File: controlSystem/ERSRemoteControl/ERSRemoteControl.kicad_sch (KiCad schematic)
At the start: 54 parts, among them J1 USB_C_Receptacle_USB2.0_14P, J2 0022-232041, J5 0022-232021, J6 0022-232021, J7 0022-232031, SW2 SW_Push, SW3 SW_Push, SW4 SW_Push, SW5 SW_Push, SW6 SW_Push, SW7 SW_Push, U1 TPS63070, U2 ESP32-S3-WROOM-1

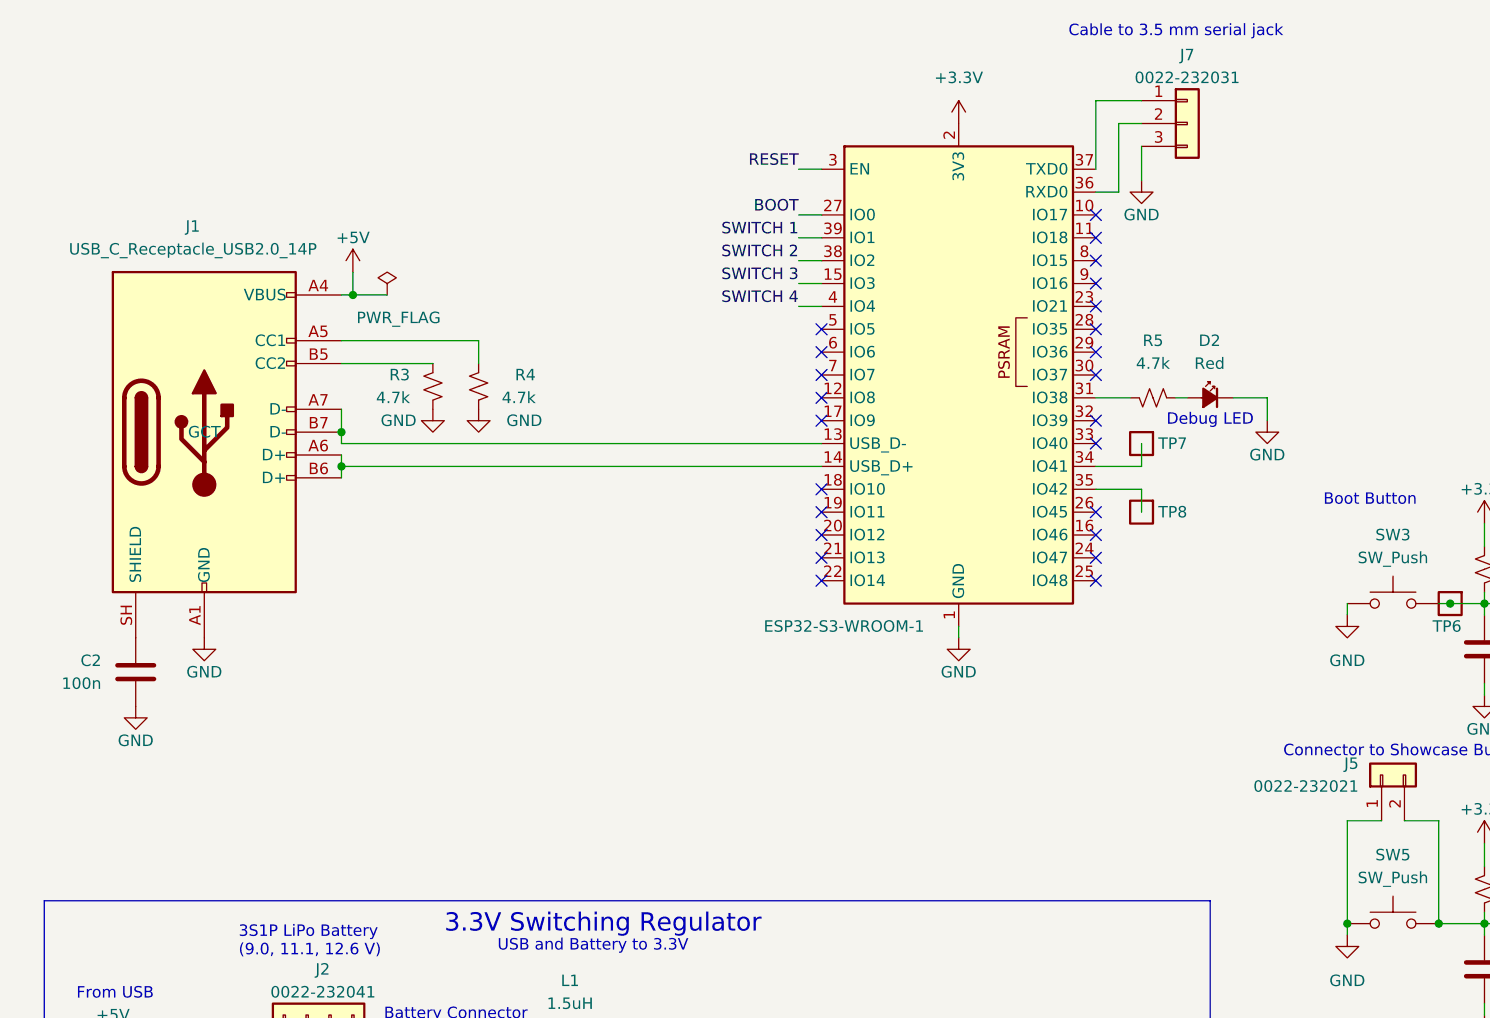
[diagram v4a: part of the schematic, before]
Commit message: Fixed traces, removed the mode switch and added debouncing logic
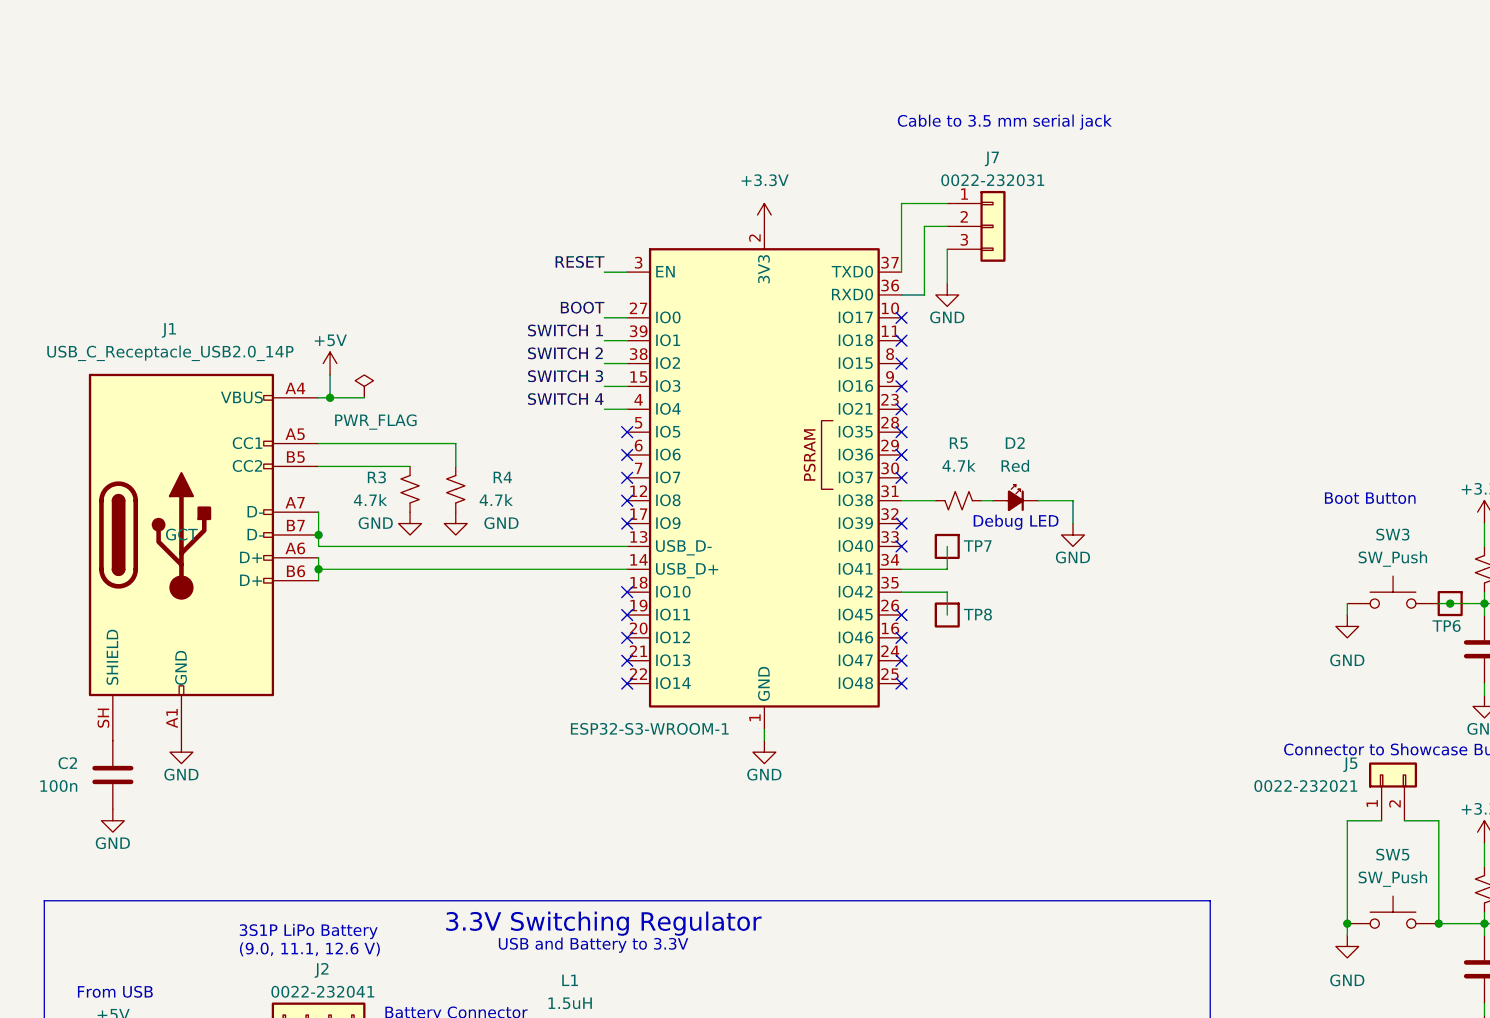
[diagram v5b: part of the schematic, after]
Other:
- moved on the sheet: C2, D2, J1, J7, R3, R4, R5, TP7, TP8

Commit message: Design review, set board constraints to osh park two layer, fix library paths, etc
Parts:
- TP1, TP2, TP3, TP4, TP5, TP6, TP7, TP8: symbol psas-testpoint:Test-Point -> Connector:TestPoint_Square
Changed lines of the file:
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@@
 	)
 	(symbol
-		(lib_id "psas-testpoint:Test-Point")
+		(lib_id "Connector:TestPoint_Square")
 		(at 118.11 78.74 0)
 		(mirror y)
@@
 	)
 	(symbol
-		(lib_id "psas-testpoint:Test-Point")
+		(lib_id "Connector:TestPoint_Square")
 		(at 208.28 77.47 0)
 		(mirror y)
@@
 	)
 	(symbol
-		(lib_id "psas-testpoint:Test-Point")
+		(lib_id "Connector:TestPoint_Square")
 		(at 91.44 158.75 0)
 		(unit 1)
@@
 	)
 	(symbol
-		(lib_id "psas-testpoint:Test-Point")
+		(lib_id "Connector:TestPoint_Square")
 		(at 91.44 148.59 0)
 		(unit 1)
@@
 	)
 	(symbol
-		(lib_id "psas-testpoint:Test-Point")
+		(lib_id "Connector:TestPoint_Square")
 		(at 173.99 77.47 0)
 		(mirror y)
@@
 	)
 	(symbol
-		(lib_id "psas-testpoint:Test-Point")
+		(lib_id "Connector:TestPoint_Square")
 		(at 118.11 71.12 0)
 		(mirror y)
@@
 	)
 	(symbol
-		(lib_id "psas-testpoint:Test-Point")
+		(lib_id "Connector:TestPoint_Square")
 		(at 76.2 171.45 0)
 		(unit 1)
@@
 		(dnp no)
 		(property "Reference" "TP3"
-			(at 74.93 173.99 0)
+			(at 77.978 172.72 0)
 			(show_name no)
 			(do_not_autoplace no)
@@
 	)
 	(symbol
-		(lib_id "psas-testpoint:Test-Point")
+		(lib_id "Connector:TestPoint_Square")
 		(at 106.68 135.89 0)
 		(unit 1)

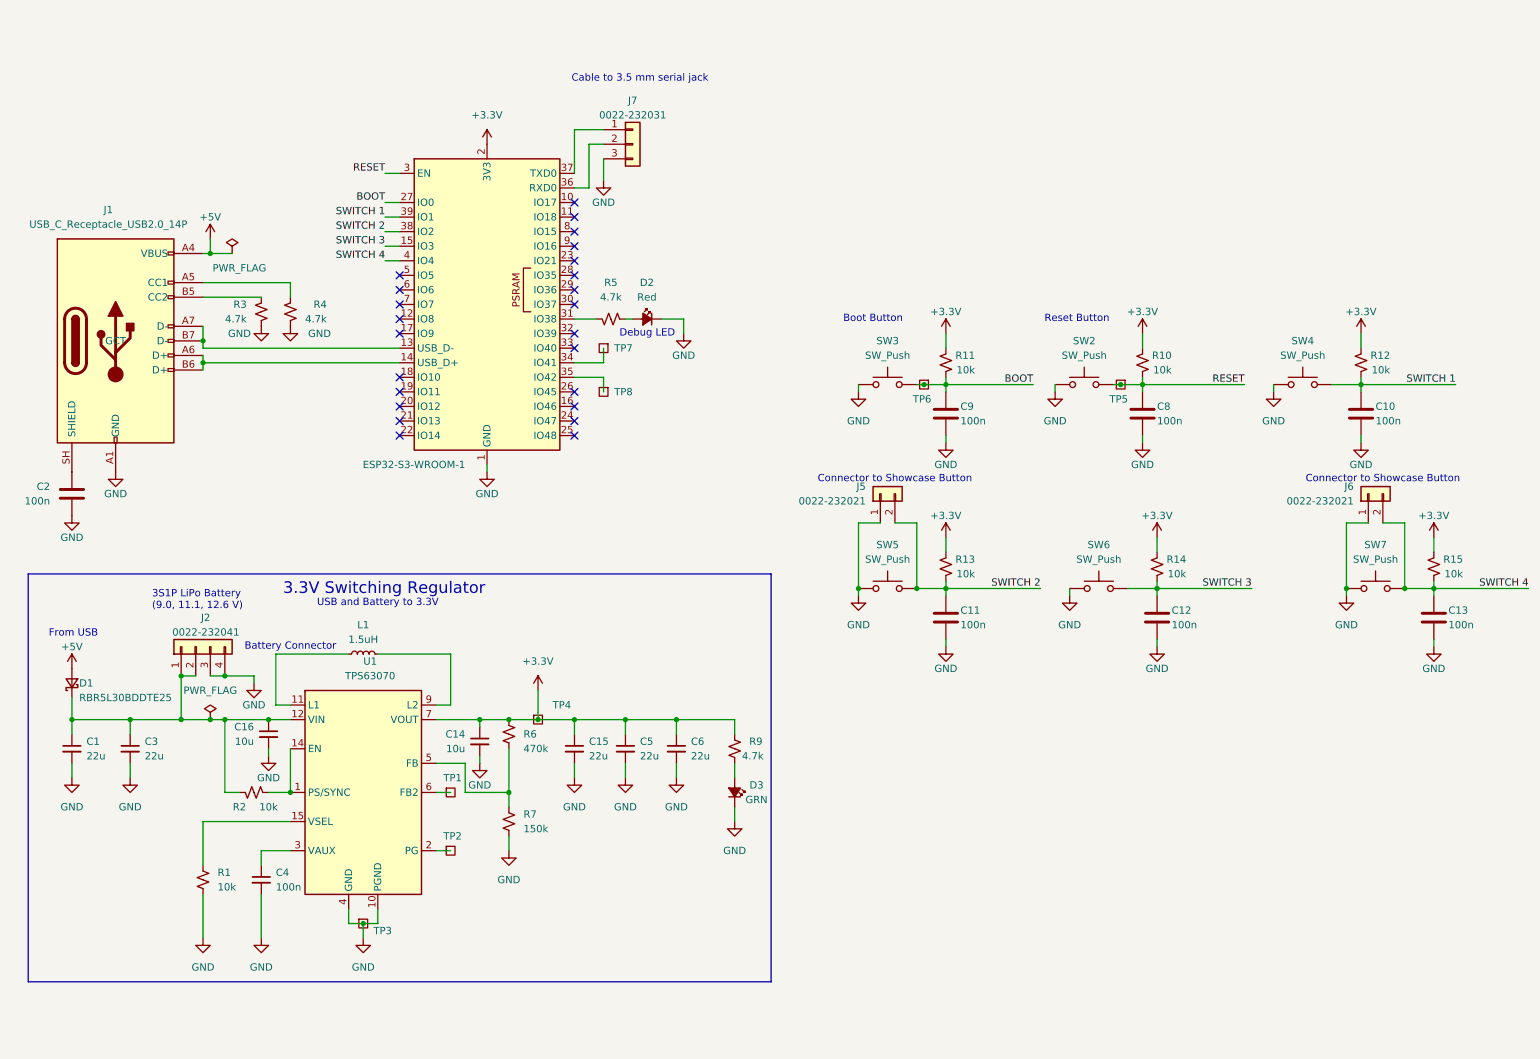
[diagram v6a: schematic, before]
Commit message: Fixed library issues and completed design review changes
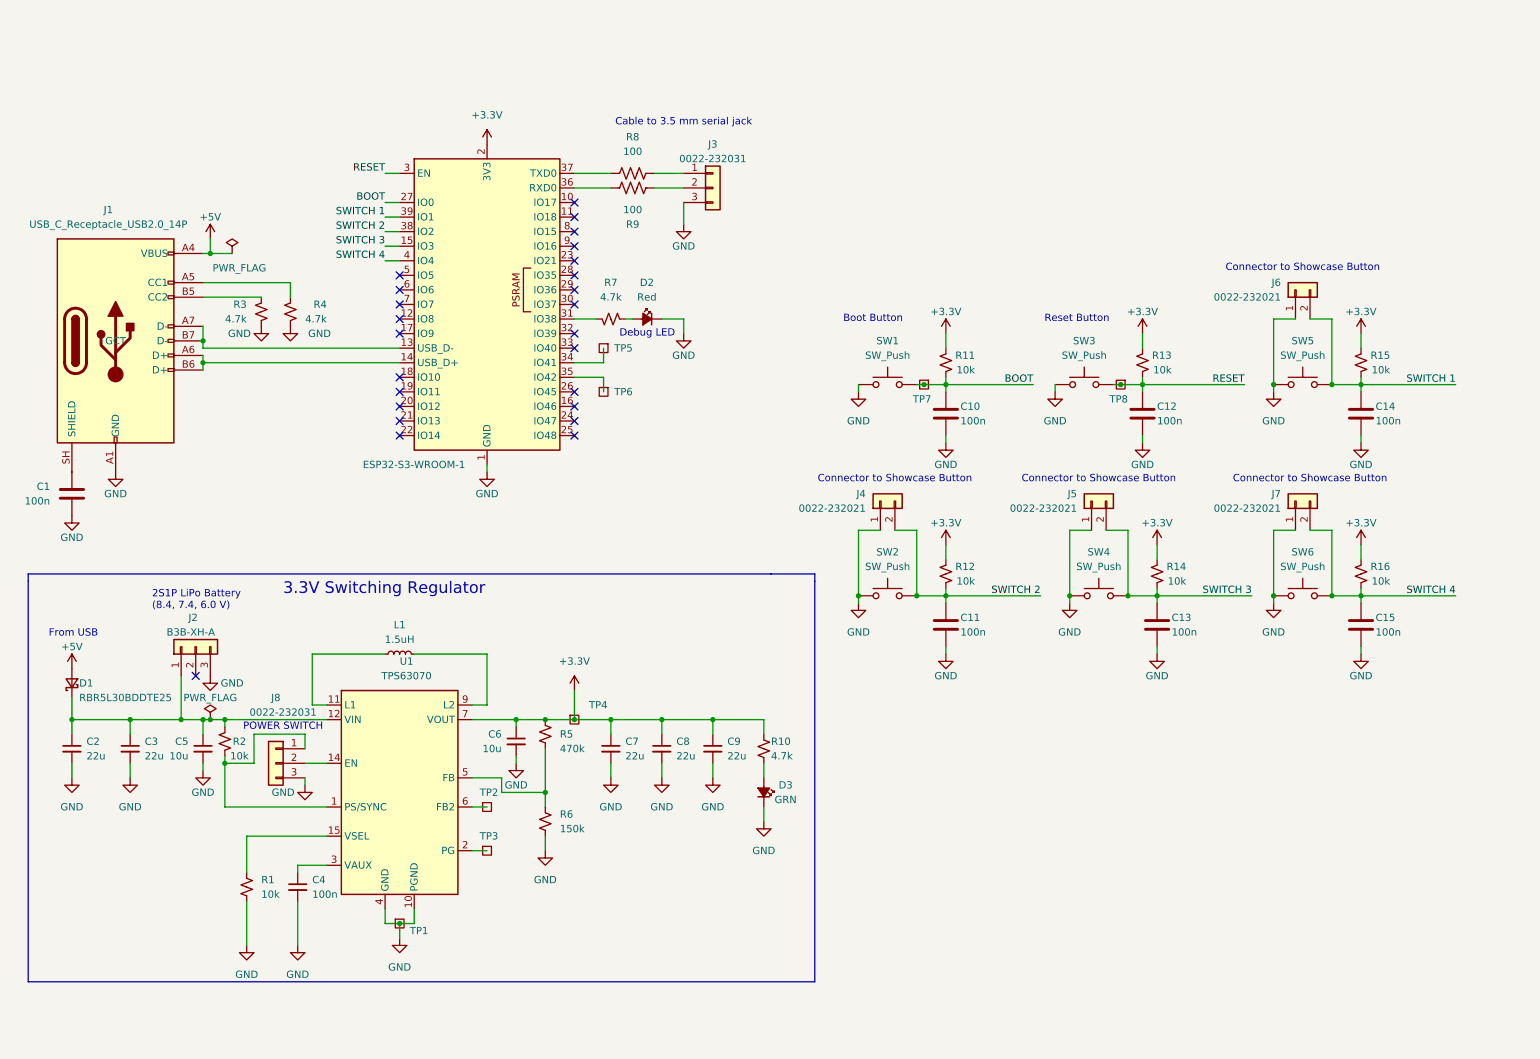
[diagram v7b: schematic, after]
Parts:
- removed J2: 0022-232041, Connector_Molex:Molex_KK-254_AE-6410-04A_1x04_P2.54mm_Vertical, symbol Connector_Generic:Conn_01x04
- added J2: B3B-XH-A, Connector_JST:JST_XH_B3B-XH-A_1x03_P2.50mm_Vertical, symbol Connector_Generic:Conn_01x03
- added J5, J6: 0022-232021, Connector_Molex:Molex_KK-254_AE-6410-02A_1x02_P2.54mm_Vertical, symbol Connector_Generic:Conn_01x02
- added J8: 0022-232031, Connector_Molex:Molex_KK-254_AE-6410-03A_1x03_P2.54mm_Vertical, symbol Connector_Generic:Conn_01x03
- added R8, R9: 100, Resistor_SMD:R_0603_1608Metric, symbol Device:R_US
- renumbered C2 to C1, C9 to C10, C8 to C12, C12 to C13, C10 to C14, C13 to C15, C1 to C2, C16 to C5, C14 to C6, C15 to C7, C5 to C8, C6 to C9, J7 to J3, J5 to J4, J6 to J7, R9 to R10, R13 to R12, R10 to R13, R12 to R15, R15 to R16, R6 to R5, R7 to R6, R5 to R7, SW3 to SW1, SW5 to SW2, SW2 to SW3, SW6 to SW4, SW4 to SW5, SW7 to SW6, TP3 to TP1, TP1 to TP2, TP2 to TP3, TP7 to TP5, TP8 to TP6, TP6 to TP7, TP5 to TP8
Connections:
- net GND: now also J2.3 (Pin_3), J5.1 (Pin_1), J6.1 (Pin_1), J8.3 (Pin_3)
- net SWITCH 1: now also J6.2 (Pin_2)
- net SWITCH 3: now also J5.2 (Pin_2)
- net at C2.1, C3.1, C5.1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: now also R2.2, J2.1 (Pin_1); no longer R2.1
- net at J3.2 (Pin_2): now also R9.1; no longer U2.36 (RXD0)
- net at U2.37 (TXD0): now also R8.1; no longer J3.1 (Pin_1)
- new net: J8.1 (Pin_1), R2.1, U1.1 (PS/SYNC)
- new net: J8.2 (Pin_2), U1.14 (EN)
- new net: J3.1 (Pin_1), R8.2
- new net: R9.2, U2.36 (RXD0)
- no-connect marks 24 -> 25
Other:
- note added: "2S1P LiPo Battery (8.4, 7.4, 6.0 V)"
- note added: "POWER SWITCH"
- note removed: "3S1P LiPo Battery (9.0, 11.1, 12.6 V)"
- note removed: "Battery Connector"
- note removed: "USB and Battery to 3.3V"
- moved on the sheet: C11, C13, C15, C4, C5, C6, C7, C8, C9, D3, J3, J4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

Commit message: Made the traces prettier but still not pretty
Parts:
- J2: DPN (none) -> 455-2248-ND; DST (none) -> DigiKey; MFR (none) -> JST; MPN (none) -> B3B-XH-A
- R8, R9: DPN (none) -> 311-100HRCT-ND; DST (none) -> DigiKey; MFR (none) -> Yageo; MPN (none) -> RC0603FR-07100RL
- TP5, TP6: now left out of the parts list
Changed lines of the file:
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@@
 		(body_style 1)
 		(exclude_from_sim no)
-		(in_bom yes)
+		(in_bom no)
 		(on_board yes)
 		(in_pos_files yes)
@@
 		(body_style 1)
 		(exclude_from_sim no)
-		(in_bom yes)
+		(in_bom no)
 		(on_board yes)
 		(in_pos_files yes)
@@
 			)
 		)
+		(property "DPN" "455-2248-ND"
+			(at 46.99 123.19 90)
+			(hide yes)
+			(show_name no)
+			(do_not_autoplace no)
+			(effects
+				(font
+					(size 1.27 1.27)
+				)
+			)
+		)
+		(property "DST" "DigiKey"
+			(at 46.99 123.19 90)
+			(hide yes)
+			(show_name no)
+			(do_not_autoplace no)
+			(effects
+				(font
+					(size 1.27 1.27)
+				)
+			)
+		)
+		(property "MFR" "JST"
+			(at 46.99 123.19 90)
+			(hide yes)
+			(show_name no)
+			(do_not_autoplace no)
+			(effects
+				(font
+					(size 1.27 1.27)
+				)
+			)
+		)
+		(property "MPN" "B3B-XH-A"
+			(at 46.99 123.19 90)
+			(hide yes)
+			(show_name no)
+			(do_not_autoplace no)
+			(effects
+				(font
+					(size 1.27 1.27)
+				)
+			)
+		)
 		(pin "3"
 		)
@@
 			)
 		)
+		(property "DPN" "311-100HRCT-ND"
+			(at 123.19 40.64 90)
+			(hide yes)
+			(show_name no)
+			(do_not_autoplace no)
+			(effects
+				(font
+					(size 1.27 1.27)
+				)
+			)
+		)
+		(property "DST" "DigiKey"
+			(at 123.19 40.64 90)
+			(hide yes)
+			(show_name no)
+			(do_not_autoplace no)
+			(effects
+				(font
+					(size 1.27 1.27)
+				)
+			)
+		)
+		(property "MFR" "Yageo"
+			(at 123.19 40.64 90)
+			(hide yes)
+			(show_name no)
+			(do_not_autoplace no)
+			(effects
+				(font
+					(size 1.27 1.27)
+				)
+			)
+		)
+		(property "MPN" "RC0603FR-07100RL"
+			(at 123.19 40.64 90)
+			(hide yes)
+			(show_name no)
+			(do_not_autoplace no)
+			(effects
+				(font
+					(size 1.27 1.27)
+				)
+			)
+		)
 		(pin "1"
 		)
@@
 			(hide yes)
 			(show_name no)
+			(do_not_autoplace no)
+			(effects
+				(font
+					(size 1.27 1.27)
+				)
+			)
+		)
+		(property "DPN" "311-100HRCT-ND"
+			(at 123.19 43.18 90)
+			(hide yes)
+			(show_name no)
+			(do_not_autoplace no)
+			(effects
+				(font
+					(size 1.27 1.27)
+				)
+			)
+		)
+		(property "DST" "DigiKey"
+			(at 123.19 43.18 90)
+			(hide yes)
+			(show_name no)
+			(do_not_autoplace no)
+			(effects
+				(font
+					(size 1.27 1.27)
+				)
+			)
+		)
+		(property "MFR" "Yageo"
+			(at 123.19 43.18 90)
+			(hide yes)
+			(show_name no)
+			(do_not_autoplace no)
+			(effects
+				(font
+					(size 1.27 1.27)
+				)
+			)
+		)
+		(property "MPN" "RC0603FR-07100RL"
+			(at 123.19 43.18 90)
+			(hide yes)
+			(show_name no)
